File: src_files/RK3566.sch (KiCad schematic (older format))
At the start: 22 parts

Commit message: littleupdate
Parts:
- removed U?: RK3566, symbol GCL_Integrated-Circuits:RK3566
- added U1: RK3566, greencharge-footprints:BGA828C65P31X31_2100X2100X161N, symbol GCL_Integrated-Circuits:RK3566
- C1, C10, C11, C12, C13, C14, C15, C16, C17, C18, C19, C2, C20, C21, C3, C4, C5, C6, C7, C8, C9: renamed from C?; footprint (none) -> Capacitor_SMD:C_0402_1005Metric
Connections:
- net GND: now also U1.1B10 (VSS30), U1.1B11 (VSS31), U1.1B15 (VSS32), U1.1B19 (VSS33), U1.1C14 (VSS39), U1.1C16 (VSS40), U1.1C18 (VSS41), U1.1C4 (VSS34), U1.1C5 (VSS35), U1.1C6 (VSS36), U1.1C8 (VSS37), U1.1C9 (VSS38), U1.1D1 (VSS42), U1.1D10 (VSS44), U1.1D14 (VSS45), U1.1D3 (VSS43), U1.1E10 (VSS48), U1.1E14 (VSS49), U1.1E15 (VSS50), U1.1E17 (VSS51), U1.1E3 (VSS46), U1.1E8 (VSS47), U1.1F10 (VSS56), U1.1F15 (VSS57), U1.1F16 (VSS58), U1.1F20 (AVSS1_6), U1.1F6 (VSS52), U1.1F7 (VSS53), U1.1F8 (VSS54), U1.1F9 (VSS55), U1.1G10 (VSS64), U1.1G11 (VSS65), U1.1G12 (VSS66), U1.1G14 (VSS67), U1.1G16 (AVSS1_7), U1.1G18 (AVSS1_8), U1.1G19 (AVSS1_9), U1.1G20 (AVSS1_10), U1.1G3 (VSS59), U1.1G6 (VSS60), U1.1G7 (VSS61), U1.1G8 (VSS62), U1.1G9 (VSS63), U1.1H1 (VSS68), U1.1H11 (VSS71), U1.1H12 (VSS72), U1.1H13 (VSS73), U1.1H2 (VSS69), U1.1H6 (VSS70), U1.1J1 (VSS74), U1.1J11 (VSS78), U1.1J12 (VSS79), U1.1J13 (VSS80), U1.1J16 (AVSS1_11), U1.1J18 (AVSS1_12), U1.1J6 (VSS75), U1.1J8 (VSS76), U1.1J9 (VSS77), U1.1K11 (VSS88), U1.1K12 (VSS89), U1.1K13 (VSS90), U1.1K14 (VSS91), U1.1K15 (VSS92), U1.1K18 (AVSS1_13), U1.1K2 (VSS81), U1.1K3 (VSS82), U1.1K4 (VSS83), U1.1K5 (VSS84), U1.1K6 (VSS85), U1.1K8 (SARADC_VIN1), U1.1K9 (VSS87), U1.1L10 (VSS95), U1.1L11 (VSS96), U1.1L12 (VSS97), U1.1L13 (VSS98), U1.1L14 (VSS99), U1.1L15 (VSS100), U1.1L19 (AVSS1_14), U1.1L3 (VSS93), U1.1L6 (VSS94), U1.1M10 (VSS105), U1.1M11 (VSS106), U1.1M12 (VSS107), U1.1M13 (VSS108), U1.1M14 (VSS109), U1.1M15 (VSS110), U1.1M16 (VSS111), U1.1M17 (VSS112), U1.1M20 (VSS113), U1.1M3 (VSS101), U1.1M4 (VSS102), U1.1M5 (VSS103), U1.1M6 (VSS104), U1.1N11 (AVSS9), U1.1N12 (AVSS10), U1.1N3 (VSS114), U1.1N4 (VSS115), U1.1N7 (VSS116), U1.1P1 (VSS117), U1.1P10 (AVSS12), U1.1P14 (AVSS13), U1.1P15 (VSS121), U1.1P5 (VSS118), U1.1P6 (VSS119), U1.1P7 (VSS120), U1.1P8 (AVSS11), U1.1R11 (AVSS16), U1.1R12 (AVSS17), U1.1R13 (AVSS18), U1.1R14 (AVSS19), U1.1R15 (AVSS20), U1.1R3 (VSS122), U1.1R4 (VSS123), U1.1R5 (VSS124), U1.1R6 (VSS125), U1.1R7 (VSS126), U1.1R8 (AVSS14), U1.1R9 (AVSS15), U1.1T10 (AVSS24), U1.1T11 (AVSS25), U1.1T12 (AVSS26), U1.1T13 (AVSS27), U1.1T14 (AVSS28), U1.1T15 (AVSS29), U1.1T17 (AVSS30), U1.1T3 (VSS127), U1.1T5 (VSS128), U1.1T7 (AVSS21), U1.1T8 (AVSS22), U1.1T9 (AVSS23), U1.1U2 (VSS129), U1.1V1 (VSS130), U1.1V12 (AVSS32), U1.1V13 (AVSS33), U1.1V18 (AVSS34), U1.1V4 (VSS131), U1.1V7 (AVSS31), U1.A1 (VSS1), U1.A2 (VSS2), U1.A38 (VSS3), U1.AA2 (VSS18), U1.AC37 (VSS24), U1.AD2 (VSS19), U1.AE37 (VSS25), U1.AH37 (VSS26), U1.AL37 (VSS27), U1.AP13 (AVSS1), U1.AP16 (AVSS2), U1.AP19 (AVSS3), U1.AP2 (VSS20), U1.AP22 (AVSS4), U1.AP25 (AVSS5), U1.AP28 (AVSS6), U1.AP31 (AVSS7), U1.AP34 (AVSS8), U1.AP37 (VSS28), U1.AP8 (VSS22), U1.AR1 (VSS21), U1.AR38 (VSS29), U1.B1 (VSS4), U1.B11 (VSS7), U1.B14 (VSS8), U1.B18 (VSS9), U1.B2 (VSS5), U1.B21 (VSS10), U1.B28 (VSS11), U1.B31 (VSS12), U1.B6 (VSS6), U1.D2 (VSS13), U1.E37 (VSS23), U1.H37 (AVSS1_1), U1.J2 (VSS14), U1.L2 (VSS15), U1.L37 (AVSS1_2), U1.P37 (AVSS1_3), U1.U2 (VSS16), U1.U37 (AVSS1_4), U1.W2 (VSS17), U1.Y37 (AVSS1_5)
- net VDD_CPU: now also U1.1C12 (VDD_CPU1), U1.1D11 (VDD_CPU2), U1.1D12 (VDD_CPU_3), U1.1E11 (VDD_CPU_4), U1.1E12 (VDD_CPU_5), U1.1E13 (VDD_CPU_6), U1.1F11 (VDD_CPU_7), U1.1F12 (VDD_CPU_8), U1.1F13 (VDD_CPU_9), U1.1F14 (VDD_CPU_10), U1.1G13 (VDD_CPU_11)
- net VDD_GPU: now also U1.1L8 (VDD_GPU_1), U1.1L9 (VDD_GPU_2), U1.1M7 (VDD_GPU_3), U1.1M8 (VDD_GPU_4), U1.1M9 (VDD_GPU_5)
- net VDD_LOGIC: now also U1.1H10 (VDD_LOGIC_4), U1.1H7 (VDD_LOGIC_1), U1.1H8 (VDD_LOGIC_2), U1.1H9 (VDD_LOGIC_3), U1.1J10 (VDD_LOGIC_6), U1.1J7 (VDD_LOGIC_5), U1.1K10 (VDD_LOGIC_8), U1.1K7 (VDD_LOGIC_7), U1.1L7 (VDD_LOGIC_9)
- net VDD_NPU: now also U1.1G15 (VDD_NPU_1), U1.1H14 (VDD_NPU_2), U1.1H15 (VDD_NPU_3), U1.1J14 (VDD_NPU_4), U1.1J15 (VDD_NPU_5)

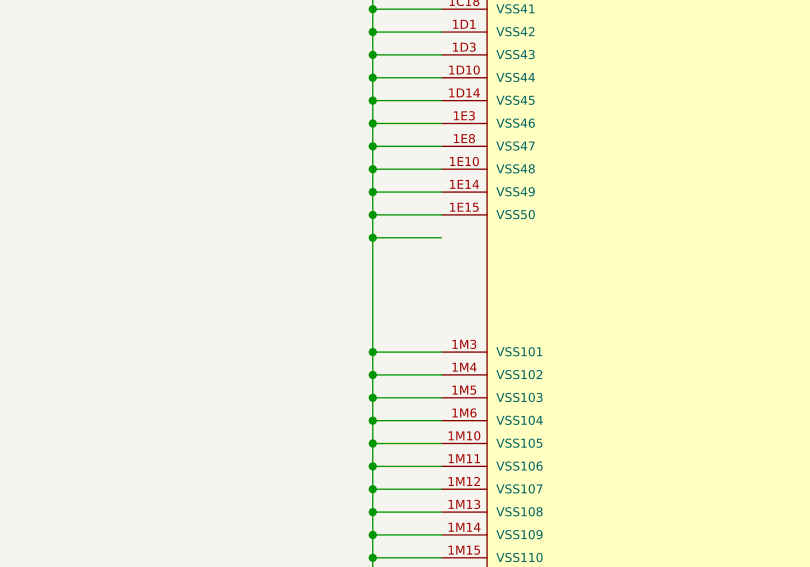
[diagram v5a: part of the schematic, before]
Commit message: schematic capture complete
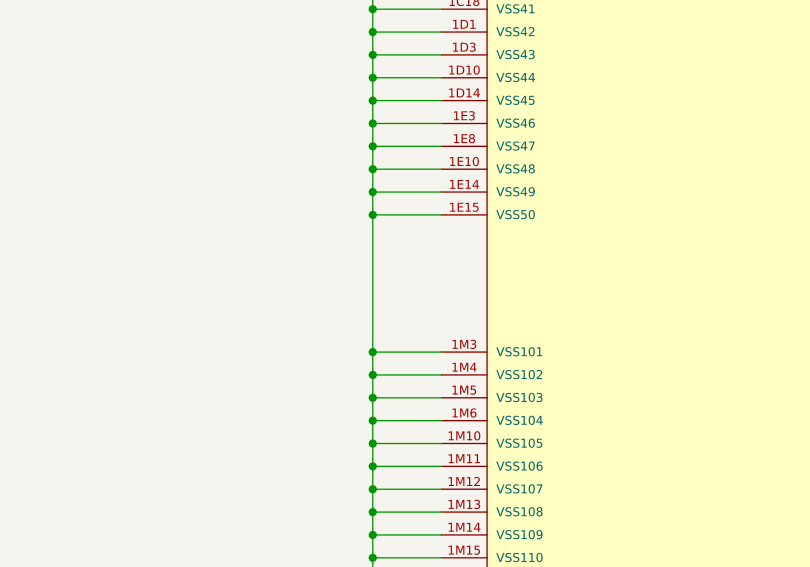
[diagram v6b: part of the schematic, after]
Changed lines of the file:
@@
 $Descr A3 16535 11693
 encoding utf-8
-Sheet 2 13
+Sheet 2 15
 Title ""
 Date ""
@@
 	4475 9800 4475 9900
 Connection ~ 4475 9900
-Wire Wire Line
-	4475 6400 4475 6900
-Connection ~ 4475 6400
-Wire Wire Line
-	4475 6300 4475 6400
 Connection ~ 4475 6300
 Wire Wire Line
@@
 Wire Wire Line
 	8825 1700 9125 1700
-Wire Wire Line
-	4475 6400 4775 6400
 Wire Wire Line
 	4775 6300 4475 6300
@@
 	1    0    0    -1
 $EndComp
+Wire Wire Line
+	4475 6300 4475 6900
 $EndSCHEMATC

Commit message: updated footprint and schematics
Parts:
- U1: footprint greencharge-footprints:BGA828C65P31X31_2100X2100X161N -> greencharge-footprints:RK366_BGA-565_20x18_15.5x14.4mm
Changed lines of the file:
@@
 $Descr A3 16535 11693
 encoding utf-8
-Sheet 2 15
+Sheet 2 16
 Title ""
 Date ""
@@
 F 0 "U1" H 6250 -575 50  0000 C CNN
 F 1 "RK3566" H 6250 -675 50  0000 C CNN
-F 2 "greencharge-footprints:BGA828C65P31X31_2100X2100X161N" H 6225 700 50  0001 C CNN
+F 2 "greencharge-footprints:RK366_BGA-565_20x18_15.5x14.4mm" H 6225 700 50  0001 C CNN
 F 3 "" H 6225 700 50  0001 C CNN
 	1    6775 800
